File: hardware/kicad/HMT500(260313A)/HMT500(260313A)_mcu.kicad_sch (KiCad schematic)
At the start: 7 parts, among them J2 TC2030-IDC-NL, U4 STM32G0B1CCT3

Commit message: Schematic v0.8: apply datasheet review A-O (HMT500(260313A))
- Real pinouts from manufacturer datasheets: LMR36006BRNXR (RNX-12),
  TPS26611DDFR (SOT-23-8), PCAP04 (QFN24); TPS2660 PowerPAD = RTN
- TPS2660: RTN isolated from GND (R22, R7 removed); R5/R6/C4/MODE on
  EF_RTN; R6 80.6k (149 mA); R5 41.2k -> OVP 29 V, supply 12-28 V so
  TPS26611 +Vs stays <= 30 V
- DAC SPI: per-DAC SCLK gating (74LVC2G32, SPI2 mode 3, LATCH1/2 on
  PB10/PB11) - daisy chain was removed in DAC8760 rev D
- DAC AVDD 10R series, ALARM wired-OR with 10k pull-up (PB6)
- Output TVS -> TVS3301 (stacked-pin two-terminal symbol)
- PCAP04 on dedicated SPI3 (PB3/4/5), VDD18 4.7uF, VDD33 10uF
- Buck per datasheet: L 15uH, COUT 2x22uF, CFF 20pF
- Shared VIN_P bulk (C53, C26 removed); PWR_FLT PB7; SGOOD -> PC6/PC7
- Parts list, circuit-design, decision log #26, review doc updated;
  netlist 74/74, 0 errors; tests pass

Co-Authored-By: Claude Opus 5.5 <noreply@anthropic.com>
Claude-Session: https://claude.ai/code/session_01JA2o8uJsqp9Vzsg4b665ev
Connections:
- net PWR_FLT: now also U4.46 (PB7); no longer U4.43 (PB4)
- net CDC_MOSI: now reaches U4.44 (PB5)
- net DAC_ALARM: now reaches U4.45 (PB6)
- net DAC1_ALARM renamed DAC2_LATCH
- net DAC2_ALARM renamed CDC_SCK
- net DAC_LATCH renamed DAC1_LATCH
- net OUT1_FLT renamed OUT1_SGOOD
- net OUT2_FLT renamed OUT2_SGOOD
- new net CDC_MISO: U4.43 (PB4)
- no-connect marks 23 -> 20
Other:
- note added: "Cortex-M0+ 64 MHz, 플래시 256 KB, RAM 144 KB, -40–125 °C, LQFP48, 내부 온도센서 (PCB 온도). SPI1 = ADS1220, SPI2 = DAC (모드 3, SCLK 게이트), SPI3 = PCAP04"
- note added: "PWR_FLT: internal pull-up (PB7)"
- note added: "SGOOD push-pull, low = OK"
- note removed: "(PB3-4, PB11, PC6-7 internal)"
- note removed: "Cortex-M0+ 64 MHz, 플래시 256 KB, RAM 144 KB, -40–125 °C, LQFP48, 내부 온도센서 (PCB 온도), SPI1 = 측정 · SPI2 = DAC 전용"
- note removed: "Fault lines: MCU pull-ups"

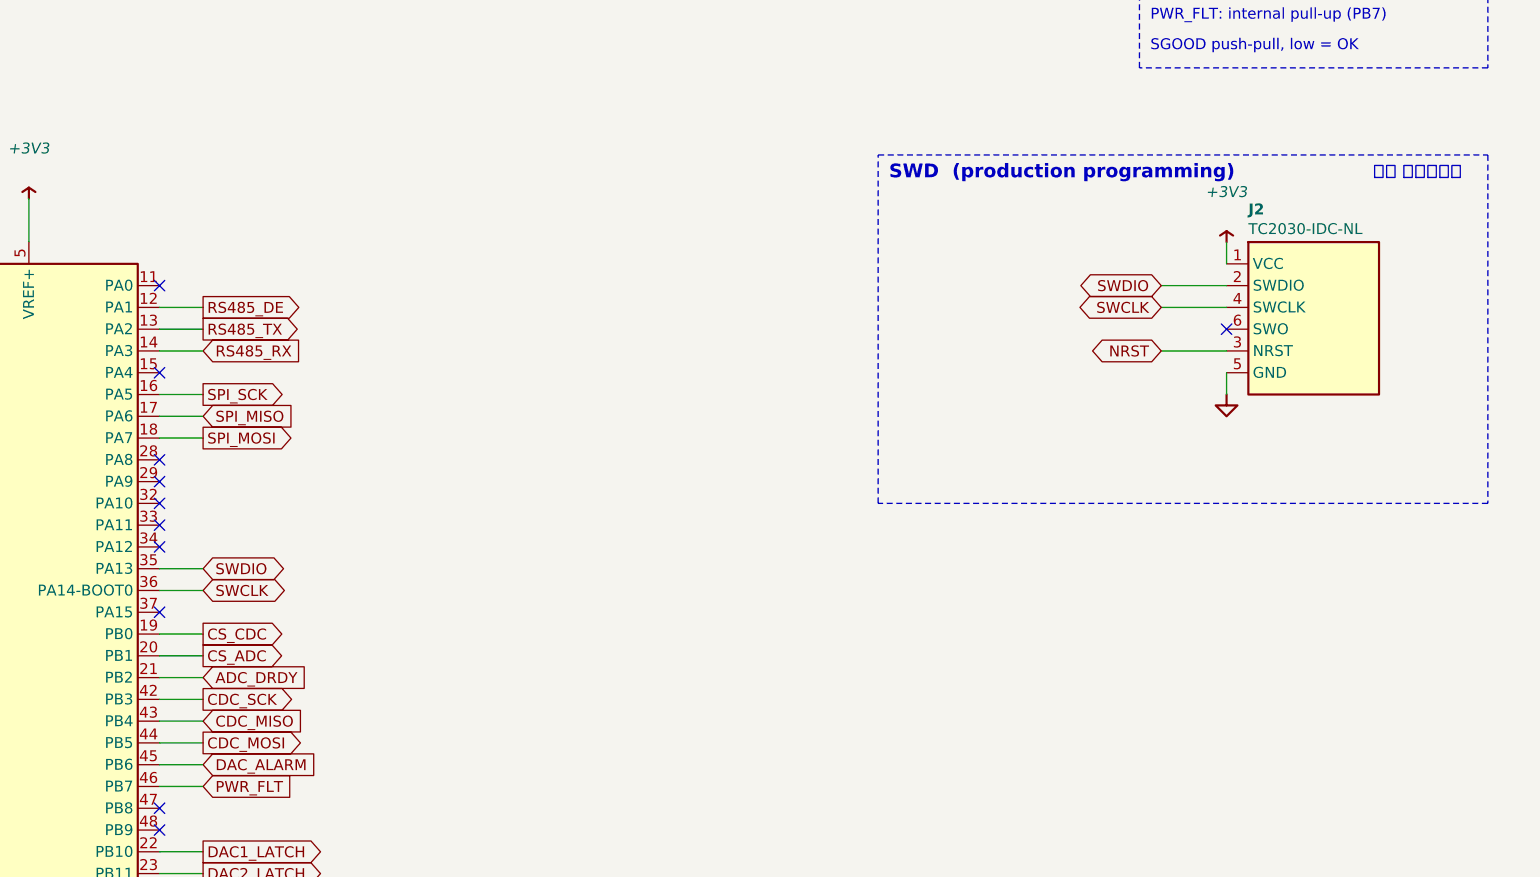
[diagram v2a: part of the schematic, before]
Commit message: Schematic: wire nearby same-sheet nets, signal-flow direction for analog nets
- Analog: +VSENSE and terminal feedback drawn as wires to the OPA197
  buffer (no DACn_SENSE / second OUTn_EXT labels); U14 1A/2A tied, one
  DAC_SCK label
- Power: TPS2660 left pins reordered so R3-R5 run straight from IN to
  UVLO/OVP; one VIN_F label
- Measurement: C27 sits directly between R17/R18 and AIN1/AIN2
- MCU: SWD pads (J2) placed on the PA13/PA14 rows and wired directly
- Label direction for passive nets from signal flow: OUTn_EXT analog ->
  connector, VIN_F connector -> eFuse, BUCK_FB divider -> FB
- Tests: nearby same-sheet labels must be wired; bend limit 6/sheet;
  check_netlist accepts KiCad auto-named multi-pin nets

Co-Authored-By: Claude Opus 5.5 <noreply@anthropic.com>
Claude-Session: https://claude.ai/code/session_01JA2o8uJsqp9Vzsg4b665ev
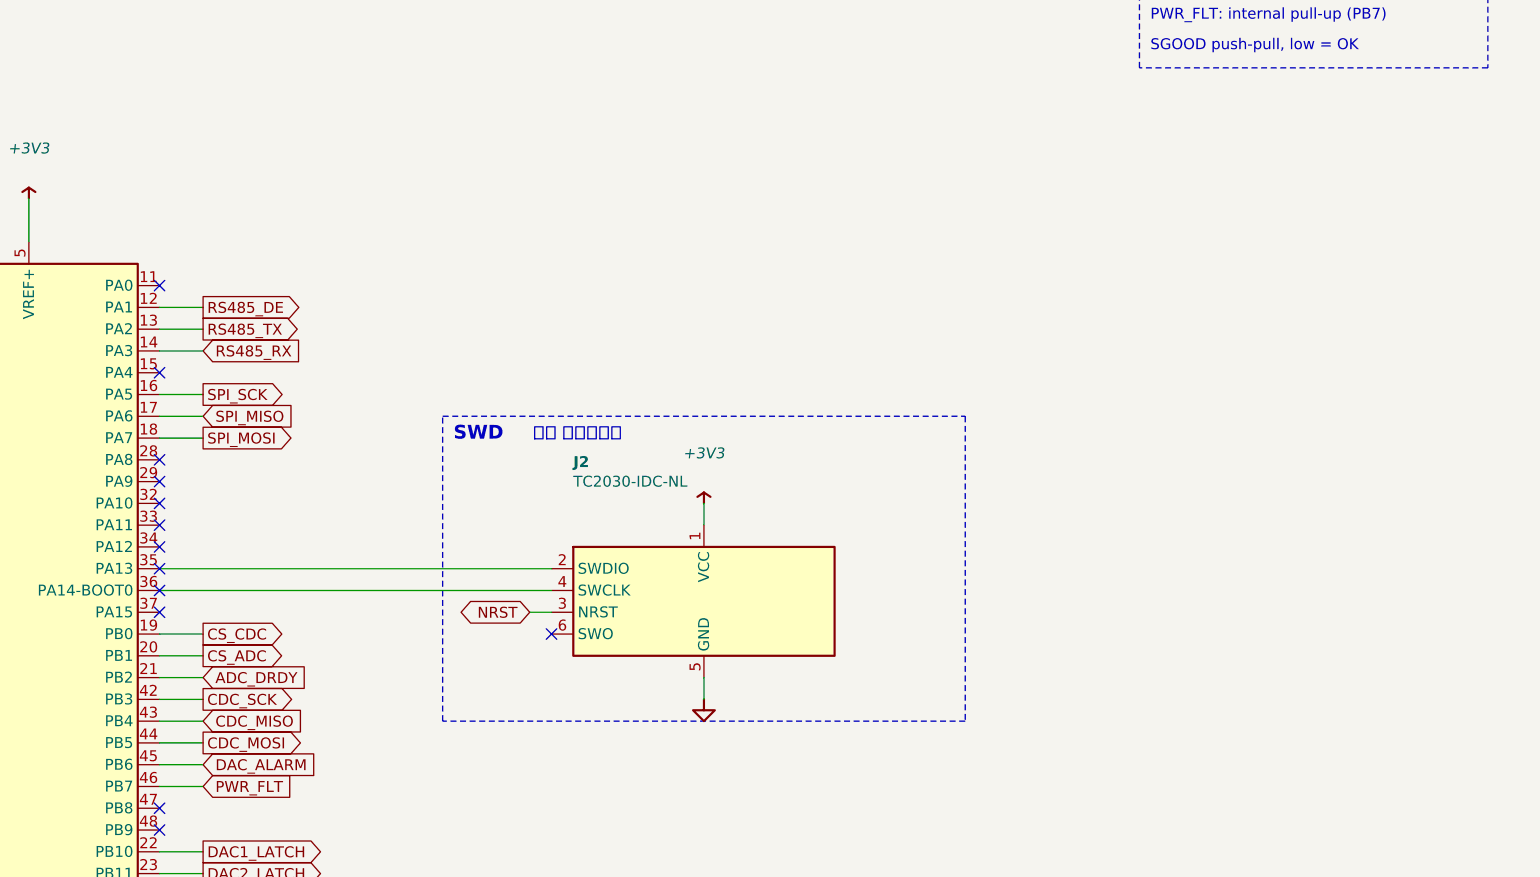
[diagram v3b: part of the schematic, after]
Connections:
- net SWCLK: no longer names the net of J2.4 (SWCLK), U4.36 (PA14-BOOT0)
- net SWDIO: no longer names the net of J2.2 (SWDIO), U4.35 (PA13)
- no-connect marks 20 -> 22
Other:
- note added: "SWD"
- note removed: "SWD (production programming)"
- moved on the sheet: J2

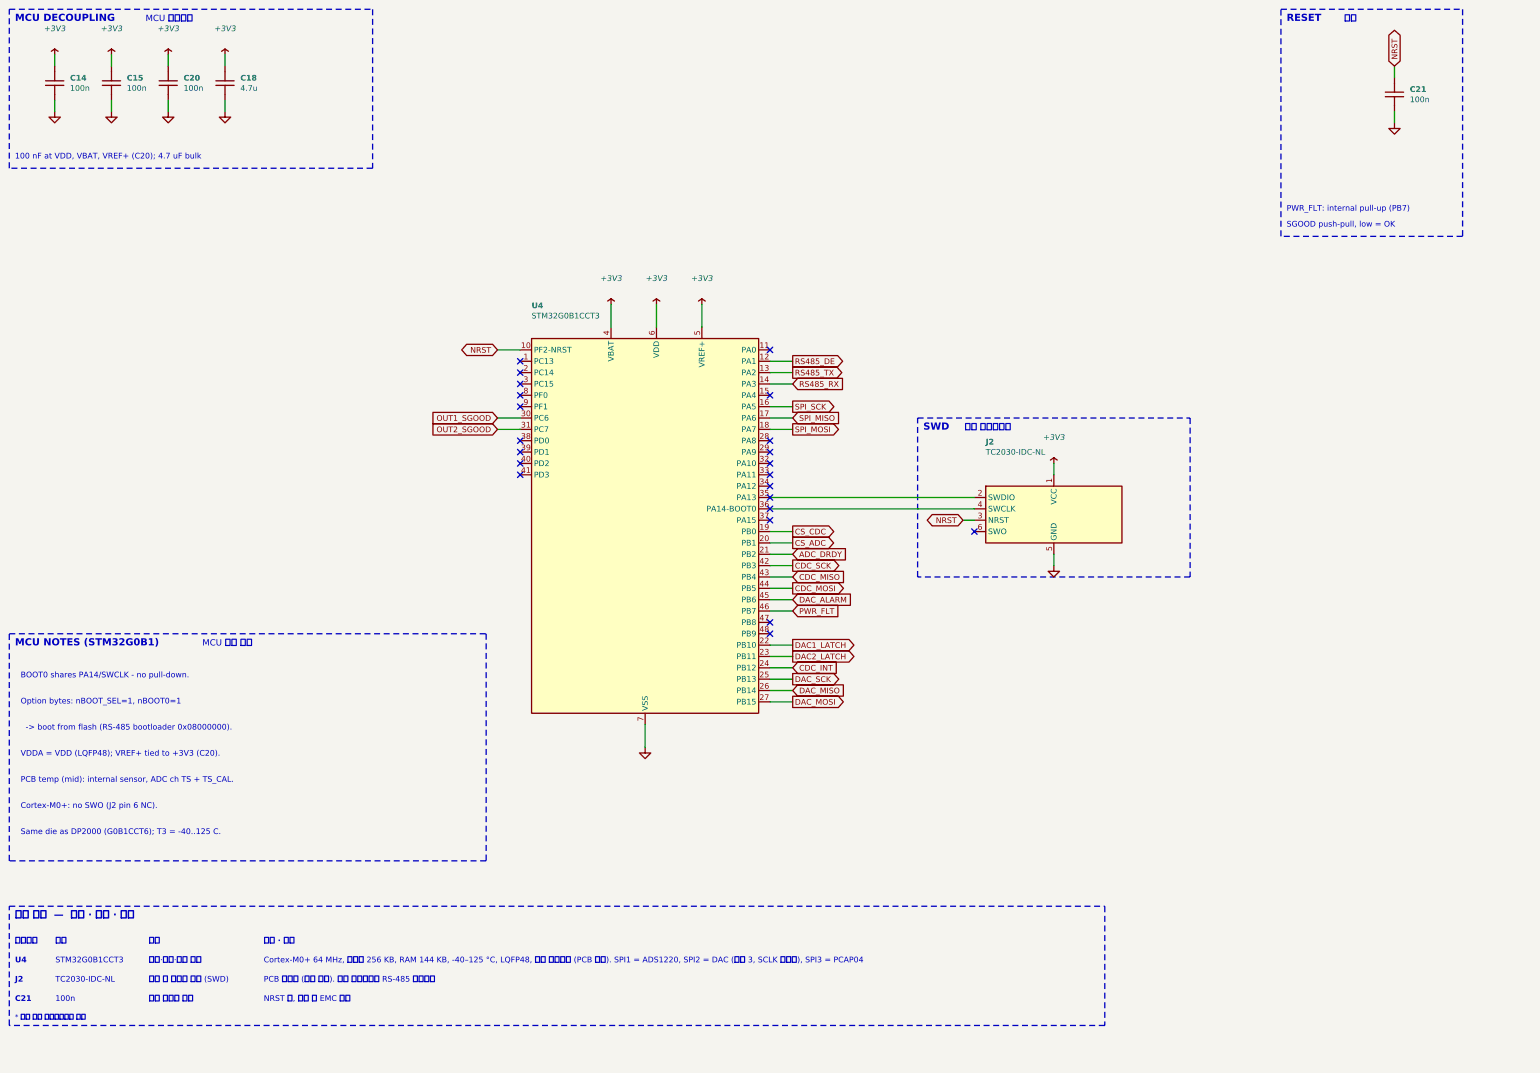
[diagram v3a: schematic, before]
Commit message: Schematic v0.9 + placement rev 4: apply triple-review A/B items, re-review fixes
- Power: OVP 32.6 V (R5 36.5k), D2 TVS3301, C2 2.2u 100V, buck input 220n x2,
  U2 pin 3 = SW; TPS26611 +Vs emitter-follower clamp (Q1 MMBTA06, R50, D50 27V)
- RS-485: THVD2410, DE 10k pull-down (R60) for in-house bootloader
- MCU: SGOOD on PA0/PA4, CS_CDC PA15, VIN_SENSE PB0, LATCH/CS pull-ups,
  SWD no-connect removed, netlist checker flags no-connect on used pins
- Analog: OPA197 V+ = DAC AVDD, R31/R41 100k, local caps; X7R throughout
- New aux sheet; SOT-23 and R1206 footprints; parts list and JLC files
- Placement: pin-targeted hints, MCU decaps under U4, chassis parts grouped
  in front, J5 keep-out 3.3 mm, CHASSIS netclass; 102/102 parts placed
- Docs: final review H table, decision #32, circuit design, placement rev 4

Co-Authored-By: Claude Opus 5.5 <noreply@anthropic.com>
Claude-Session: https://claude.ai/code/session_01JA2o8uJsqp9Vzsg4b665ev
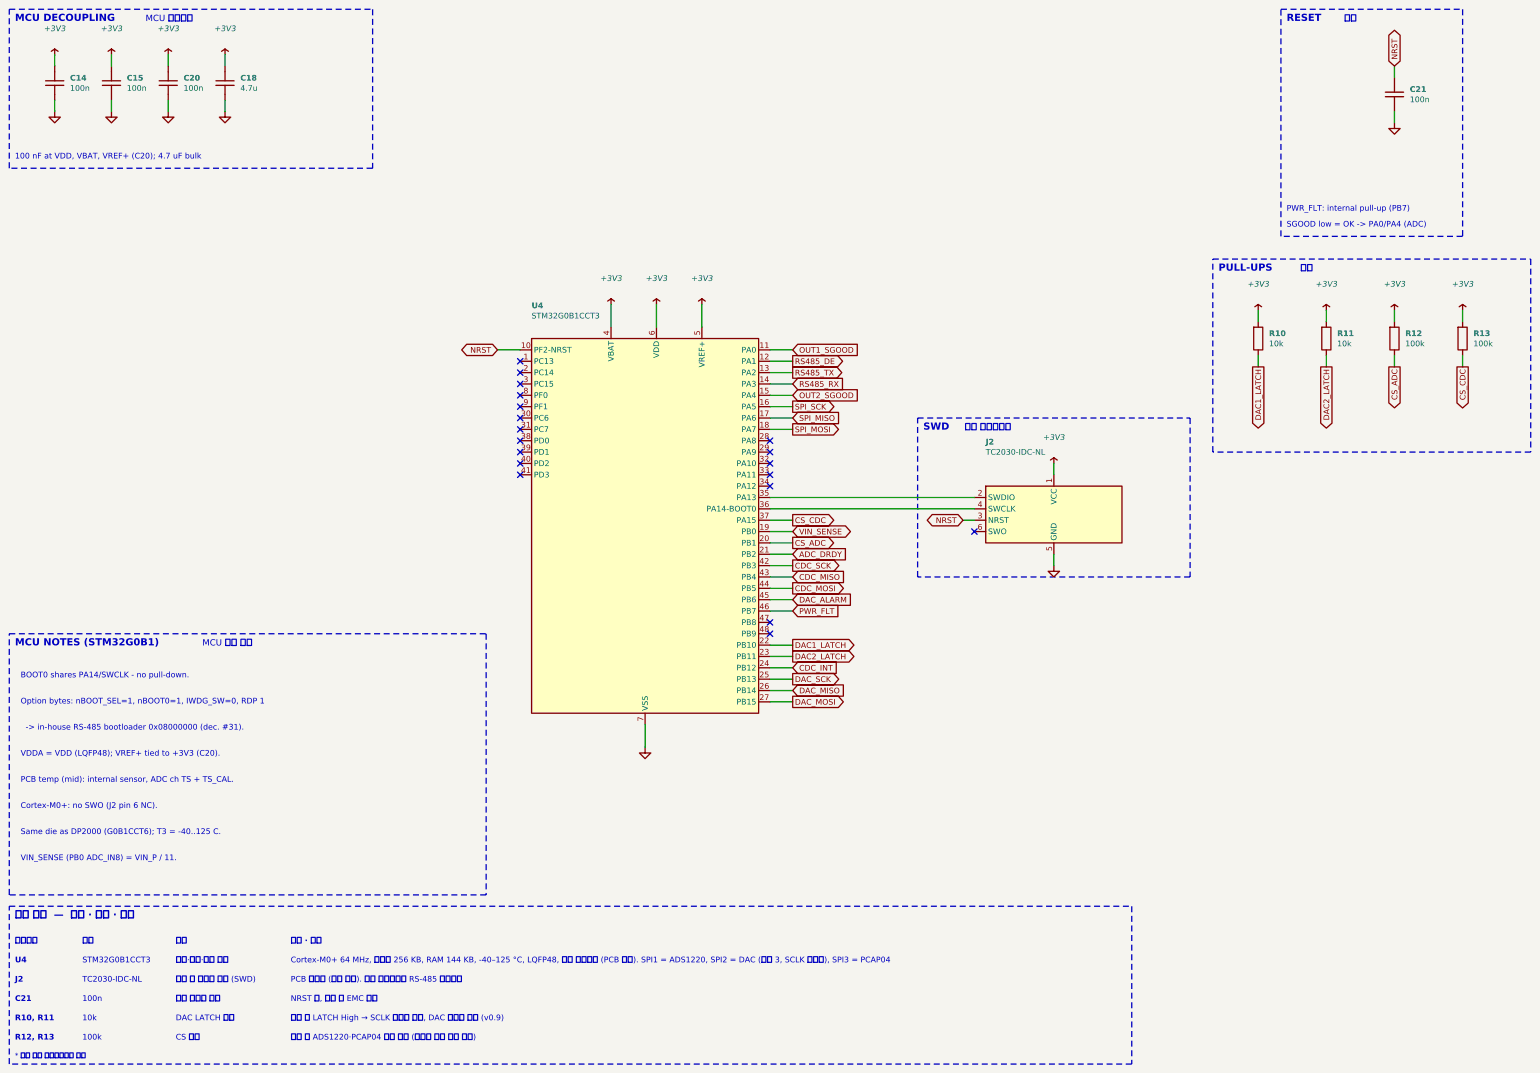
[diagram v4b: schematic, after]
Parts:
- added R10, R11: 10k, Resistor_SMD:R_0603_1608Metric, symbol HMT500_260313A:R
- added R12, R13: 100k, Resistor_SMD:R_0603_1608Metric, symbol HMT500_260313A:R
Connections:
- net +3V3: now also R10.1, R11.1, R12.1, R13.1
- net CS_ADC: now also R12.2
- net CS_CDC: now also U4.37 (PA15), R13.2; no longer U4.19 (PB0)
- net DAC1_LATCH: now also R10.2
- net DAC2_LATCH: now also R11.2
- net OUT1_SGOOD: now also U4.11 (PA0); no longer U4.30 (PC6)
- net OUT2_SGOOD: now also U4.15 (PA4); no longer U4.31 (PC7)
- new net VIN_SENSE: U4.19 (PB0)
- no-connect marks 22 -> 19
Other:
- note added: "-> in-house RS-485 bootloader 0x08000000 (dec. #31)."
- note added: "100k"
- note added: "10k"
- note added: "CS 풀업"
- note added: "DAC LATCH 풀업"
- note added: "Option bytes: nBOOT_SEL=1, nBOOT0=1, IWDG_SW=0, RDP 1"
- note added: "PULL-UPS"
- note added: "R10, R11"
- note added: "R12, R13"
- note added: "SGOOD low = OK -> PA0/PA4 (ADC)"
- note added: "VIN_SENSE (PB0 ADC_IN8) = VIN_P / 11."
- note added: "리셋 중 ADS1220·PCAP04 선택 해제 (디지털 입력 부동 금지)"
- note added: "리셋 중 LATCH High → SCLK 게이트 닫힘, DAC 오입력 방지 (v0.9)"
- note added: "풀업"
- note removed: "-> boot from flash (RS-485 bootloader 0x08000000)."
- note removed: "Option bytes: nBOOT_SEL=1, nBOOT0=1"
- note removed: "SGOOD push-pull, low = OK"

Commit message: Apply agreed external review items (decision #35)
- H01: series 100 V Schottky D3 (PMEG10010ELR) between D2 and eFuse IN
  (new net VIN_D) so negative surges no longer stress U1 IN-OUT
- H02: RS-485 bus TVS D60/D61 (TVS3301); U11 -> THVD2410DGKR (VSSOP-8)
- H04: +Vs clamp zener 27 V -> 24 V (BZX84C24LT1G)
- H08: ADS1220 IDAC fixed at 250 uA
- Room for new parts: C7 removed, 37 low-voltage R/C moved to 0402
  (LCSC basic where available); chassis parts keep CH_GAP between each other
- Placement 104/104, netlist 78/78, pcbnew DRC: no clearance errors,
  assembly sim 23 OK; parts list / JLC BOM updated
- docs/hw/external-review-response-260930.md: item responses, output load
  table, current budget, firmware requirements F1-F6, tests T1-T7

Co-Authored-By: Claude Opus 5.5 <noreply@anthropic.com>
Claude-Session: https://claude.ai/code/session_01JA2o8uJsqp9Vzsg4b665ev
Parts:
- C14, C15, C20, C21: footprint Capacitor_SMD:C_0603_1608Metric -> Capacitor_SMD:C_0402_1005Metric
- R10, R11, R12, R13: footprint Resistor_SMD:R_0603_1608Metric -> Resistor_SMD:R_0402_1005Metric
